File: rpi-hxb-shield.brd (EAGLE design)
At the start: 31.5 x 55 mm, 33 parts, among them Q1 CRYSTALX22, U2 24LC32A/SN, X1 MICROMATCH-8

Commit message: removal of unneeded micromatch connector
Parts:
- removed X1: MICROMATCH-8, con-amp-micromatch:MICROMATCH-8
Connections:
- removed net RXD: X1.7
- removed net TCK: X1.2
- removed net TDI: X1.5
- removed net TDO: X1.4
- removed net TMS: X1.3
- removed net TXD: X1.8
- net GND: no longer X1.6
- net VCC: no longer X1.1
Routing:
- net TCK: track 30.1 -> 0.00 mm, vias 1 -> 0
- net TMS: track 26.6 -> 0.00 mm, vias 1 -> 0
- net VCC: track 107.9 -> 82.9 mm
- net TDO: track 23.1 -> 0.00 mm, vias 1 -> 0
- net RXD: track 22.4 -> 0.00 mm, vias 1 -> 0
- net TDI: track 21.7 -> 0.00 mm, vias 1 -> 0
- net TXD: track 20.9 -> 0.00 mm, vias 1 -> 0
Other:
- board text removed: "BTN"
- board text removed: "GND"
- board text removed: "MISO"
- board text removed: "MOSI"
- board text removed: "PA0"
- board text removed: "PA1"
- board text removed: "PA2"
- board text removed: "PA3"
- board text removed: "PA4"
- board text removed: "PA5"
- board text removed: "PA6"
- board text removed: "PA7"
- board text removed: "PB0"
- board text removed: "PB1"
- board text removed: "PB2"
- board text removed: "PB3"
- board text removed: "PC6"
- board text removed: "PC7"
- board text removed: "PD3"
- board text removed: "PD4"
- board text removed: "SCL"
- board text removed: "SCLK"
- board text removed: "SDA"
- board text removed: "VCC"

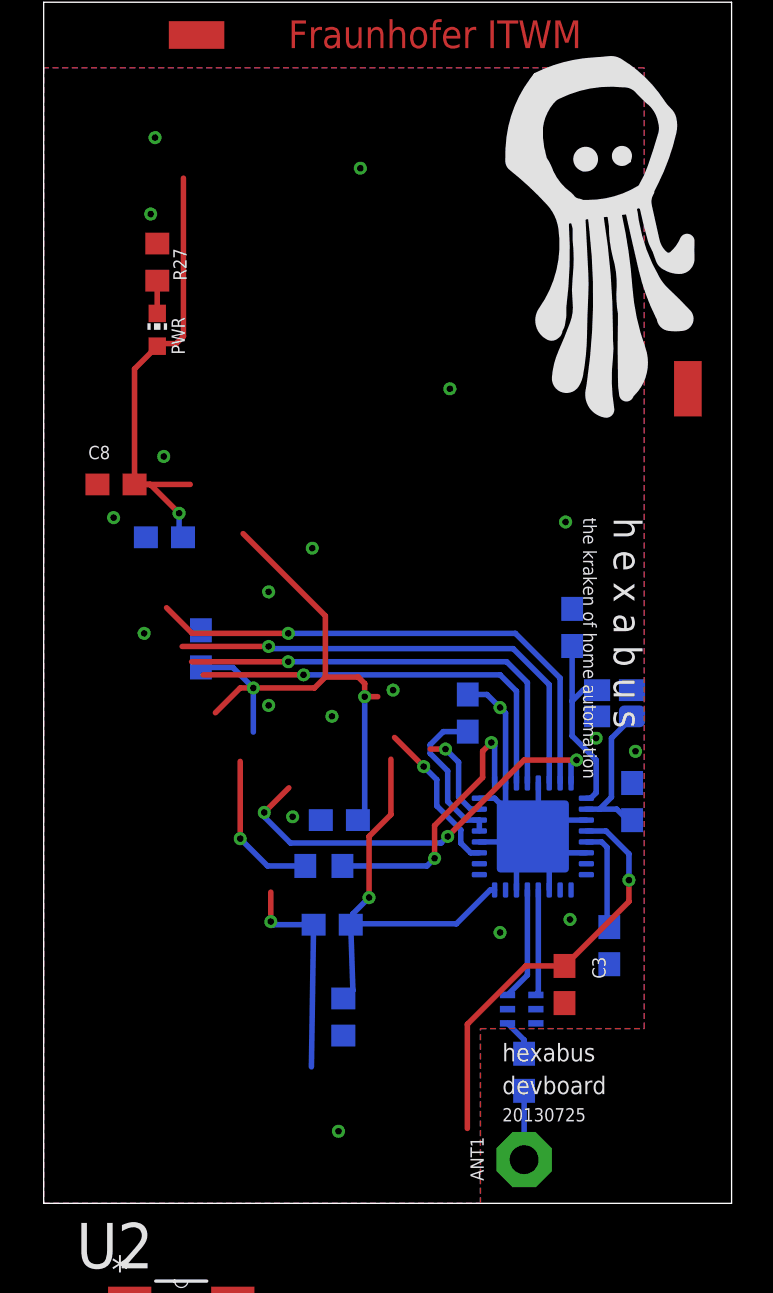
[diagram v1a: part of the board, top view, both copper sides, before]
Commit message: removal of the power LED and ripup of all wires
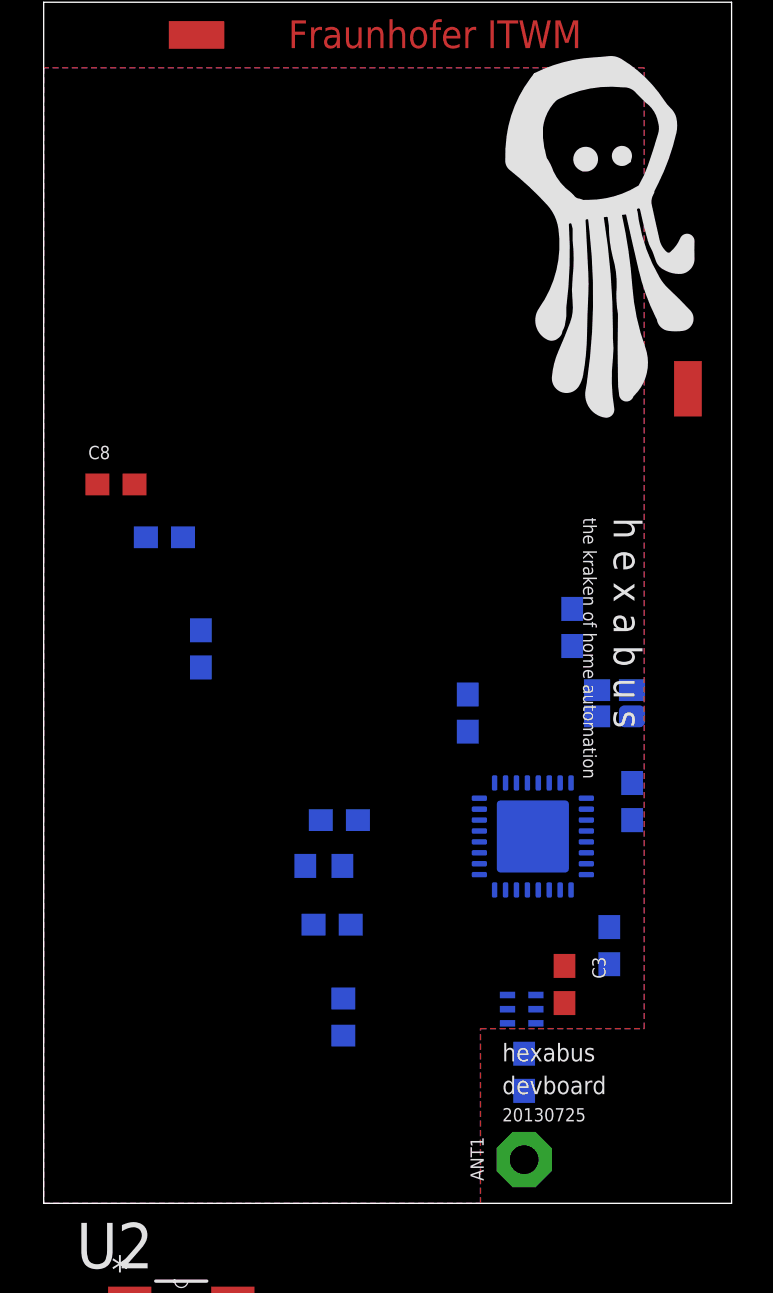
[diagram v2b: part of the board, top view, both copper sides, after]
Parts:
- removed PWR: red, led:CHIP-LED0603
- removed R27: 82R, rcl:R0603
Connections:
- removed net N$32: PWR.C, R27.2
- net GND: no longer R27.1
- net VCC: no longer PWR.A
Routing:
- net VCC: track 82.9 -> 0.00 mm, vias 6 -> 0
- net GND: track 28.8 -> 0.00 mm, vias 20 -> 0
- net SEL1: track 24.2 -> 0.00 mm, vias 1 -> 0
- net MOSI: track 22.0 -> 0.00 mm, vias 1 -> 0
- net MISO: track 20.4 -> 0.00 mm, vias 1 -> 0
- net IRQ: track 19.4 -> 0.00 mm, vias 3 -> 0
- net AT_RST: track 19.1 -> 0.00 mm, vias 1 -> 0
- net SCLK: track 18.9 -> 0.00 mm, vias 1 -> 0
- net N$5: track 12.8 -> 0.00 mm, vias 2 -> 0
- net N$31: track 9.08 -> 0.00 mm
- net N$30: track 7.31 -> 0.00 mm
- net N$2: track 7.20 -> 0.00 mm
- net SLP_TR: track 7.13 -> 0.00 mm, vias 1 -> 0
- net CLKM: track 7.04 -> 0.00 mm, vias 1 -> 0
- net N$28: track 5.19 -> 0.00 mm
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
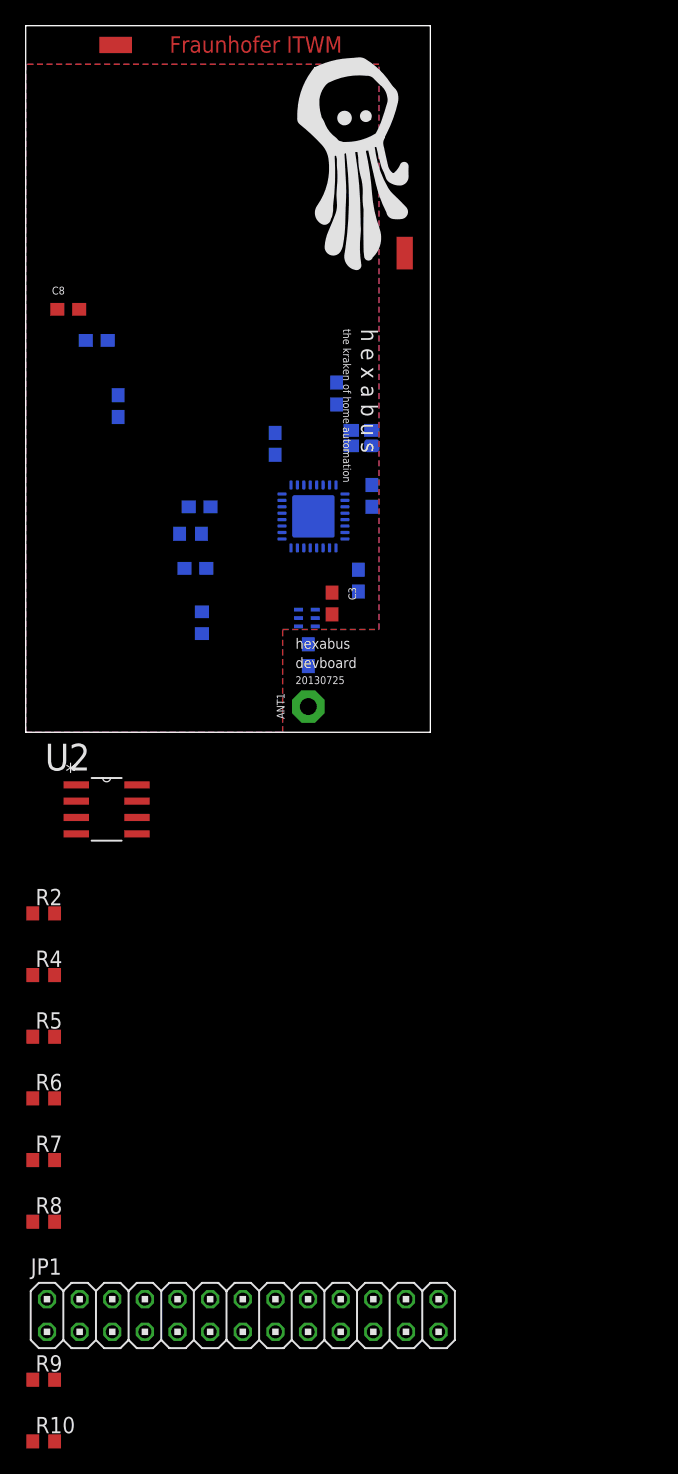
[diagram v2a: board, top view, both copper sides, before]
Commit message: swapped EEPROM to 128K variant
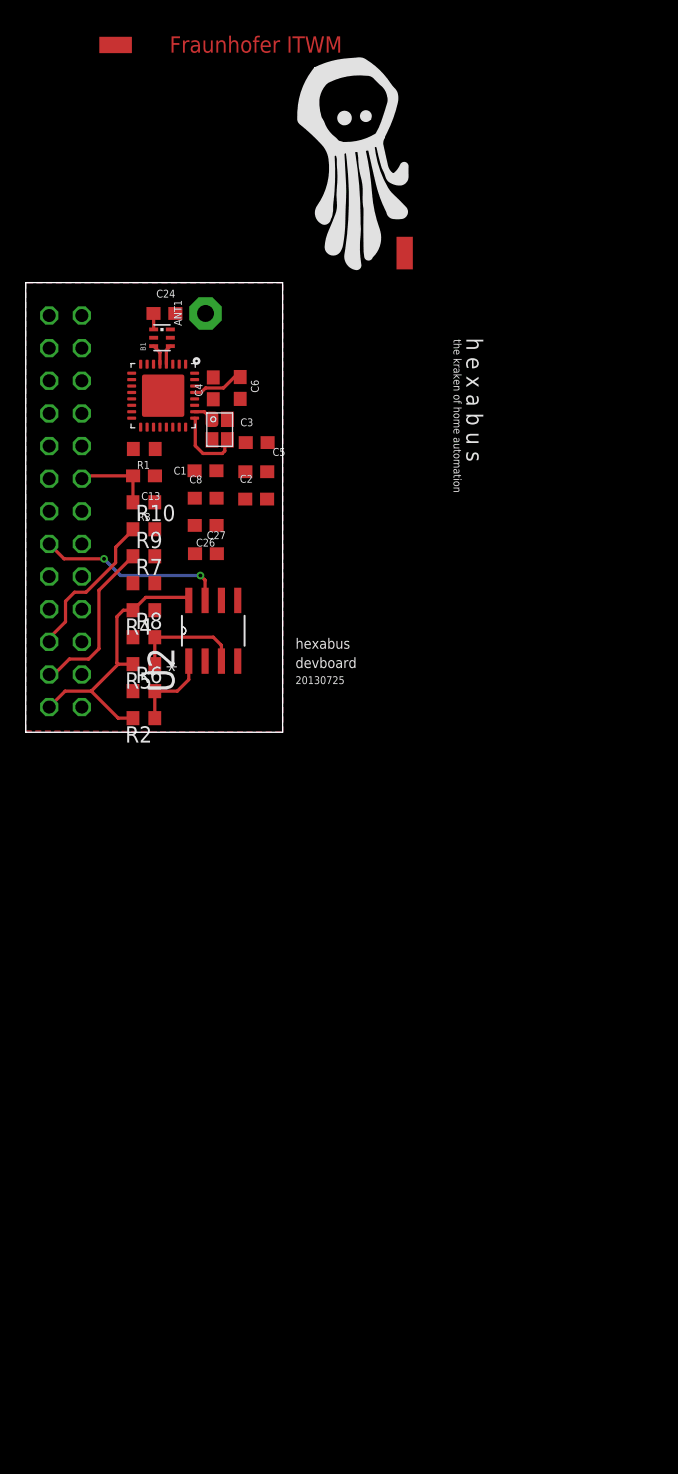
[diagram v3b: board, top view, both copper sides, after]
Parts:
- U2: value 24LC32A/SN -> 24LC128-I/SN
- moved R10 71.4 mm to (9.20, 15.8)
- moved R9 64.6 mm to (9.20, 13.7)
- moved JP1 64.1 mm to (3.10, 17.2), flipped to the bottom, turned to 90 degrees
- moved R8 46.2 mm to (9.20, 7.40)
- moved R7 45.6 mm to (9.20, 11.6)
- moved R6 32.6 mm to (9.20, 3.20)
- moved ANT1 31.6 mm to (14.0, 32.6)
- moved R5 30.0 mm to (9.20, 5.30), turned to 180 degrees
- moved R4 29.5 mm to (9.20, 9.50), turned to 180 degrees
- moved C24 28.9 mm to (10.8, 32.6), flipped to the top, turned to 0 degrees
- moved B1 24.6 mm to (10.6, 30.7), flipped to the top, turned to 90 degrees
- moved C27 18.6 mm to (14.0, 13.9), flipped to the top
- moved C8 18.2 mm to (14.0, 18.2)
- moved C6 17.6 mm to (16.7, 26.8), flipped to the top
- moved R2 17.1 mm to (9.20, 1.10), turned to 180 degrees
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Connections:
- new net WP: JP1.11, U2.7
- net GND: no longer U2.7
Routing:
- net VCC: track 0.00 -> 22.1 mm
- net WP: track 0.00 -> 14.9 mm, vias 0 -> 2
- net SDA: track 0.00 -> 13.0 mm
- net SCL: track 0.00 -> 12.0 mm
- net N$10: track 0.00 -> 8.78 mm
- net N$4: track 0.00 -> 6.56 mm
- net AT_RST: track 0.00 -> 6.15 mm
- net N$31: track 0.00 -> 5.74 mm
- net N$1: track 0.00 -> 4.05 mm
- net N$28: track 0.00 -> 1.61 mm
- net N$30: track 0.00 -> 1.59 mm
- net N$29: track 0.00 -> 1.54 mm
- net N$33: track 0.00 -> 1.25 mm
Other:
- board size 31.5 x 55 mm -> 20 x 35 mm

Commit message: prelimenary routing
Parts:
- moved C4 6.48 mm to (14.0, 20.3), turned to 0 degrees
- moved C1 6.47 mm to (14.6, 26.8), turned to 90 degrees
- moved R5 6.30 mm to (9.20, 11.6)
- moved R7 6.30 mm to (9.20, 5.30)
- moved C3 2.30 mm to (17.9, 20.2)
- moved C5 2.10 mm to (17.9, 22.4)
- moved R4 2.10 mm to (9.20, 7.40)
- moved R8 2.10 mm to (9.20, 9.50)
- turned C26 to 0 degrees
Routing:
- net VCC: track 22.1 -> 61.3 mm, vias 0 -> 4
- net MOSI: track 0.00 -> 19.6 mm, vias 0 -> 1
- net SDA: track 13.0 -> 31.3 mm, vias 0 -> 1
- net N$2: track 0.00 -> 18.2 mm
- net MISO: track 0.00 -> 17.0 mm, vias 0 -> 1
- net SCL: track 12.0 -> 27.9 mm, vias 0 -> 1
- net IRQ: track 0.00 -> 15.3 mm, vias 0 -> 1
- net SEL1: track 0.00 -> 14.8 mm, vias 0 -> 1
- net SCLK: track 0.00 -> 13.6 mm, vias 0 -> 1
- net AT_RST: track 6.15 -> 18.1 mm
- net N$9: track 0.00 -> 7.69 mm
- net SLP_TR: track 0.00 -> 6.63 mm, vias 0 -> 1
- net GND: track 0.00 -> 5.31 mm, vias 0 -> 3
- net N$34: track 0.00 -> 2.35 mm
- net N$31: track 5.74 -> 7.93 mm
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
